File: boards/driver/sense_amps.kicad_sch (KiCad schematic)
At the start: 4 parts, among them Q88 MMBT2222, U19 AD8505

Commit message: Driver: filled out the rest of the BOM, except for defaults for nominal resistances
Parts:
- R266: MPN (none) -> ERA-3ARB102V; Manufacturer (none) -> Panasonic Electronic Components; Package (none) -> 0603; Rating (none) -> 1/10W; Tolerance (none) -> 0.1%
- R267: MPN (none) -> ERA-3AEB750V; Manufacturer (none) -> Panasonic Electronic Components; Package (none) -> 0603; Rating (none) -> 1/10W; Tolerance (none) -> 0.1%
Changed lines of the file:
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@@
+      (effects (font (size 1.27 1.27)) hide)
+    )
+    (property "Tolerance" "0.1%" (id 4) (at 198.12 86.36 0)
+      (effects (font (size 1.27 1.27)) hide)
+    )
+    (property "Description" "RES SMD 1K OHM 0.1% 1/10W 0603" (id 5) (at 198.12 86.36 0)
+      (effects (font (size 1.27 1.27)) hide)
+    )
+    (property "MPN" "ERA-3ARB102V" (id 6) (at 198.12 86.36 0)
+      (effects (font (size 1.27 1.27)) hide)
+    )
+    (property "Manufacturer" "Panasonic Electronic Components" (id 7) (at 198.12 86.36 0)
+      (effects (font (size 1.27 1.27)) hide)
+    )
+    (property "Package" "0603" (id 8) (at 198.12 86.36 0)
+      (effects (font (size 1.27 1.27)) hide)
+    )
+    (property "Rating" "1/10W" (id 9) (at 198.12 86.36 0)
       (effects (font (size 1.27 1.27)) hide)
     )
@@
       (effects (font (size 1.27 1.27)) hide)
     )
+    (property "Description" "RES SMD 75 OHM 0.1% 1/10W 0603" (id 4) (at 198.12 96.52 0)
+      (effects (font (size 1.27 1.27)) hide)
+    )
+    (property "MPN" "ERA-3AEB750V" (id 5) (at 198.12 96.52 0)
+      (effects (font (size 1.27 1.27)) hide)
+    )
+    (property "Manufacturer" "Panasonic Electronic Components" (id 6) (at 198.12 96.52 0)
+      (effects (font (size 1.27 1.27)) hide)
+    )
+    (property "Package" "0603" (id 7) (at 198.12 96.52 0)
+      (effects (font (size 1.27 1.27)) hide)
+    )
+    (property "Rating" "1/10W" (id 8) (at 198.12 96.52 0)
+      (effects (font (size 1.27 1.27)) hide)
+    )
+    (property "Tolerance" "0.1%" (id 9) (at 198.12 96.52 0)
+      (effects (font (size 1.27 1.27)) hide)
+    )

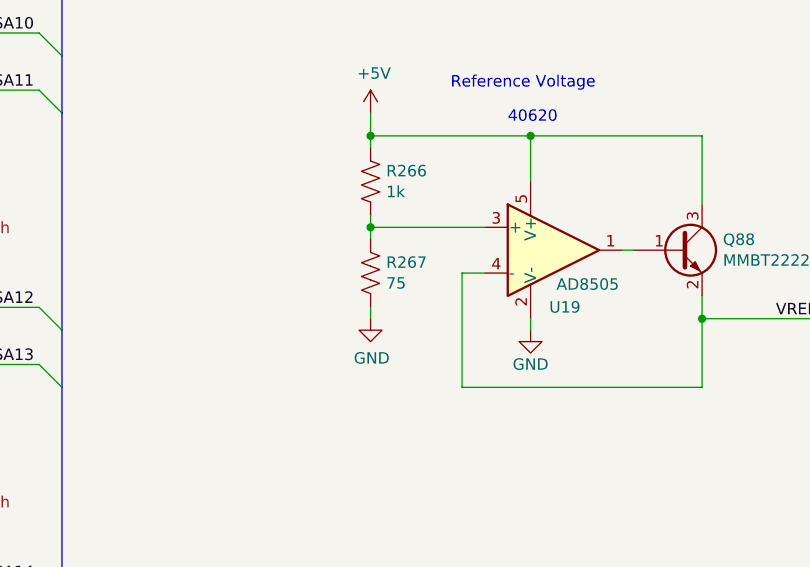
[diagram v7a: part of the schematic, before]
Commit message: Driver: corrected reference divider resistor and added diode direction symbols to the silkscreen
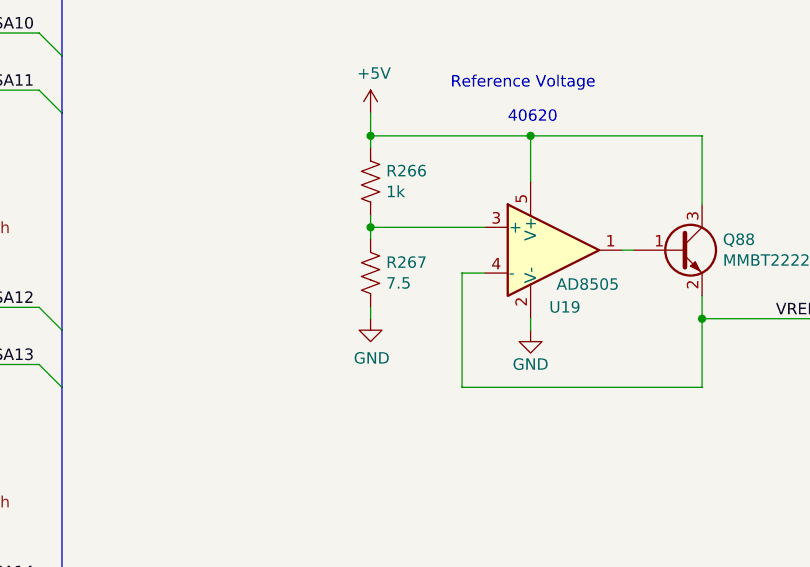
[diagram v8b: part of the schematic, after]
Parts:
- R267: value 75 -> 7.5; MPN ERA-3AEB750V -> RN73C1J7R5BTD; Manufacturer Panasonic Electronic Components -> TE Connectivity; Rating 1/10W -> 1/16W
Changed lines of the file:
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@@
       (effects (font (size 1.27 1.27)) (justify left))
     )
-    (property "Value" "75" (id 1) (at 199.8472 97.663 0)
+    (property "Value" "7.5" (id 1) (at 199.8472 97.663 0)
       (effects (font (size 1.27 1.27)) (justify left))
     )
@@
       (effects (font (size 1.27 1.27)) hide)
     )
-    (property "Description" "RES SMD 75 OHM 0.1% 1/10W 0603" (id 4) (at 198.12 96.52 0)
+    (property "Description" "RES SMD 7.5 OHM 0.1% 1/16W 0603" (id 4) (at 198.12 96.52 0)
       (effects (font (size 1.27 1.27)) hide)
     )
-    (property "MPN" "ERA-3AEB750V" (id 5) (at 198.12 96.52 0)
+    (property "MPN" "RN73C1J7R5BTD" (id 5) (at 198.12 96.52 0)
       (effects (font (size 1.27 1.27)) hide)
     )
-    (property "Manufacturer" "Panasonic Electronic Components" (id 6) (at 198.12 96.52 0)
+    (property "Manufacturer" "TE Connectivity" (id 6) (at 198.12 96.52 0)
       (effects (font (size 1.27 1.27)) hide)
     )
@@
       (effects (font (size 1.27 1.27)) hide)
     )
-    (property "Rating" "1/10W" (id 8) (at 198.12 96.52 0)
+    (property "Rating" "1/16W" (id 8) (at 198.12 96.52 0)
       (effects (font (size 1.27 1.27)) hide)
     )
